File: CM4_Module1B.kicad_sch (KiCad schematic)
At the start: 11 parts, among them J5 2340901-1

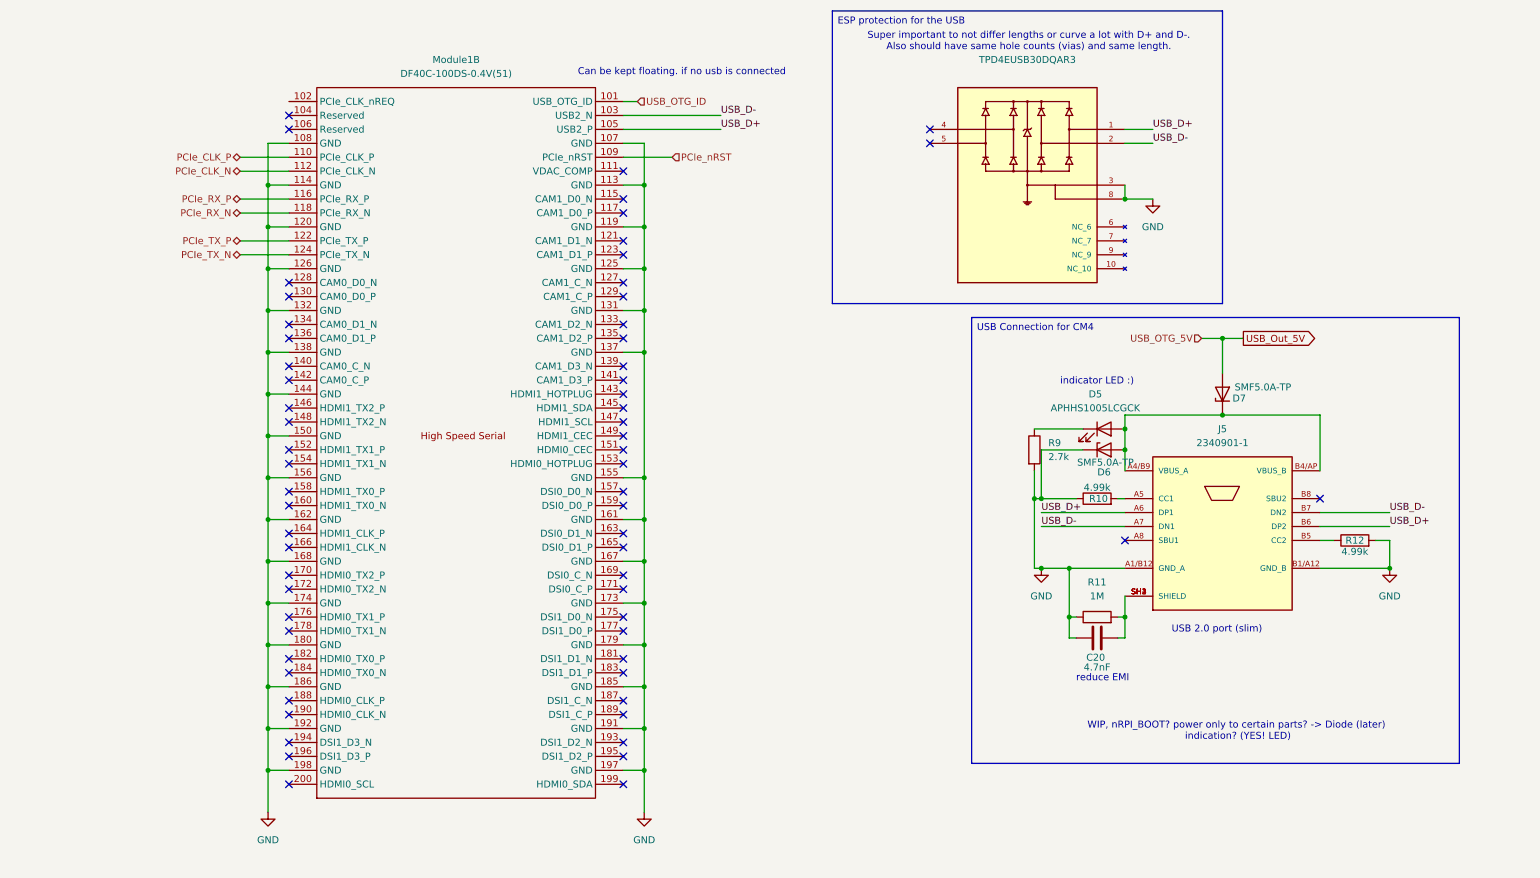
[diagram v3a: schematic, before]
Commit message: tried to find some placements for power routing
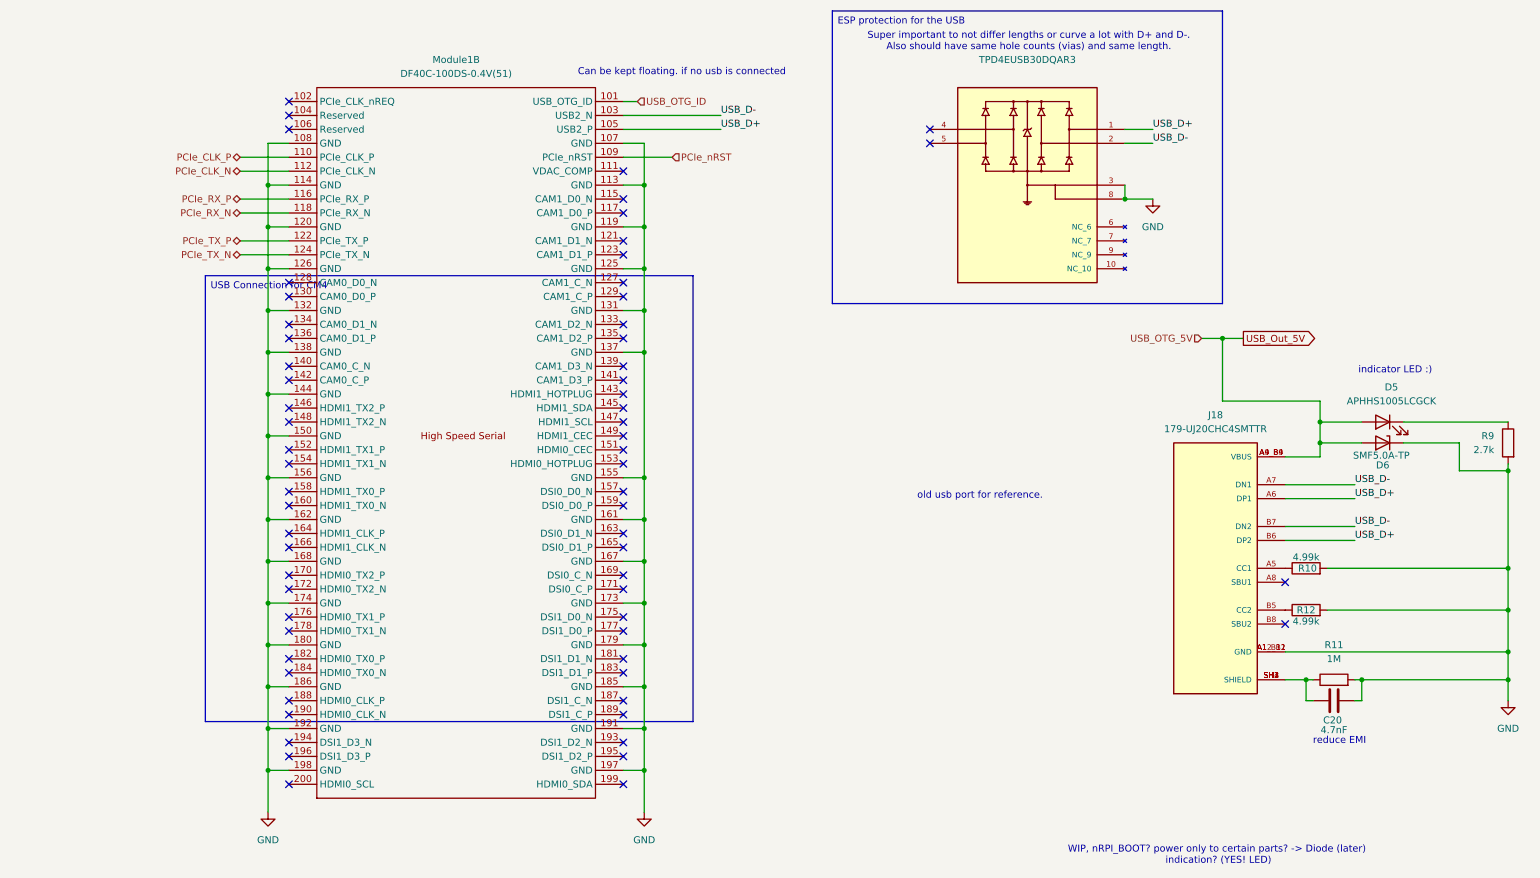
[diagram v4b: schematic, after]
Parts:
- removed D7: SMF5.0A-TP, dz_dio:SMF50ATP, symbol #dzdb:s_dio/D-MCC-SMF5.0A-TP
- removed J5: 2340901-1, dz_con:CON-TECON-2340901-1, symbol #dzdb:s_con/CON-TEC-2340901-1
- added J18: 179-UJ20CHC4SMTTR, dz_con:CON_Samesky_CUI_UJ20-C-H-C-4-SMT-TR, symbol #dzdb:s_con/SAME-179-UJ20CHC4SMTTR
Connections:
- net GND: now also C20.1, R10.2, R11.2, J18.A12_B1 (GND), J18.A1_B12 (GND); no longer C20.2, R10.1, R11.1
- net USB_D+: now also J18.A6 (DP1), J18.B6 (DP2)
- net USB_D-: now also J18.A7 (DN1), J18.B7 (DN2)
- net USB_Out_5V: now also D5.2 (A), D6.2 (A), J18.A4_B9 (VBUS), J18.A9_B4 (VBUS)
- net at R12.1: now also J18.B5 (CC2)
- new net: C20.2, J18.SH1 (SHIELD), J18.SH2 (SHIELD), J18.SH3 (SHIELD), J18.SH4 (SHIELD), R11.1
- new net: J18.A5 (CC1), R10.1
- no-connect marks 63 -> 64
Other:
- note added: "old usb port for reference."
- note removed: "USB 2.0 port (slim)"
- moved on the sheet: C20, D5, D6, R10, R11, R12, R9

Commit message: checked the whole schematic with the datasheet, took notes/questions in the datasheet (pdf also uploaded)
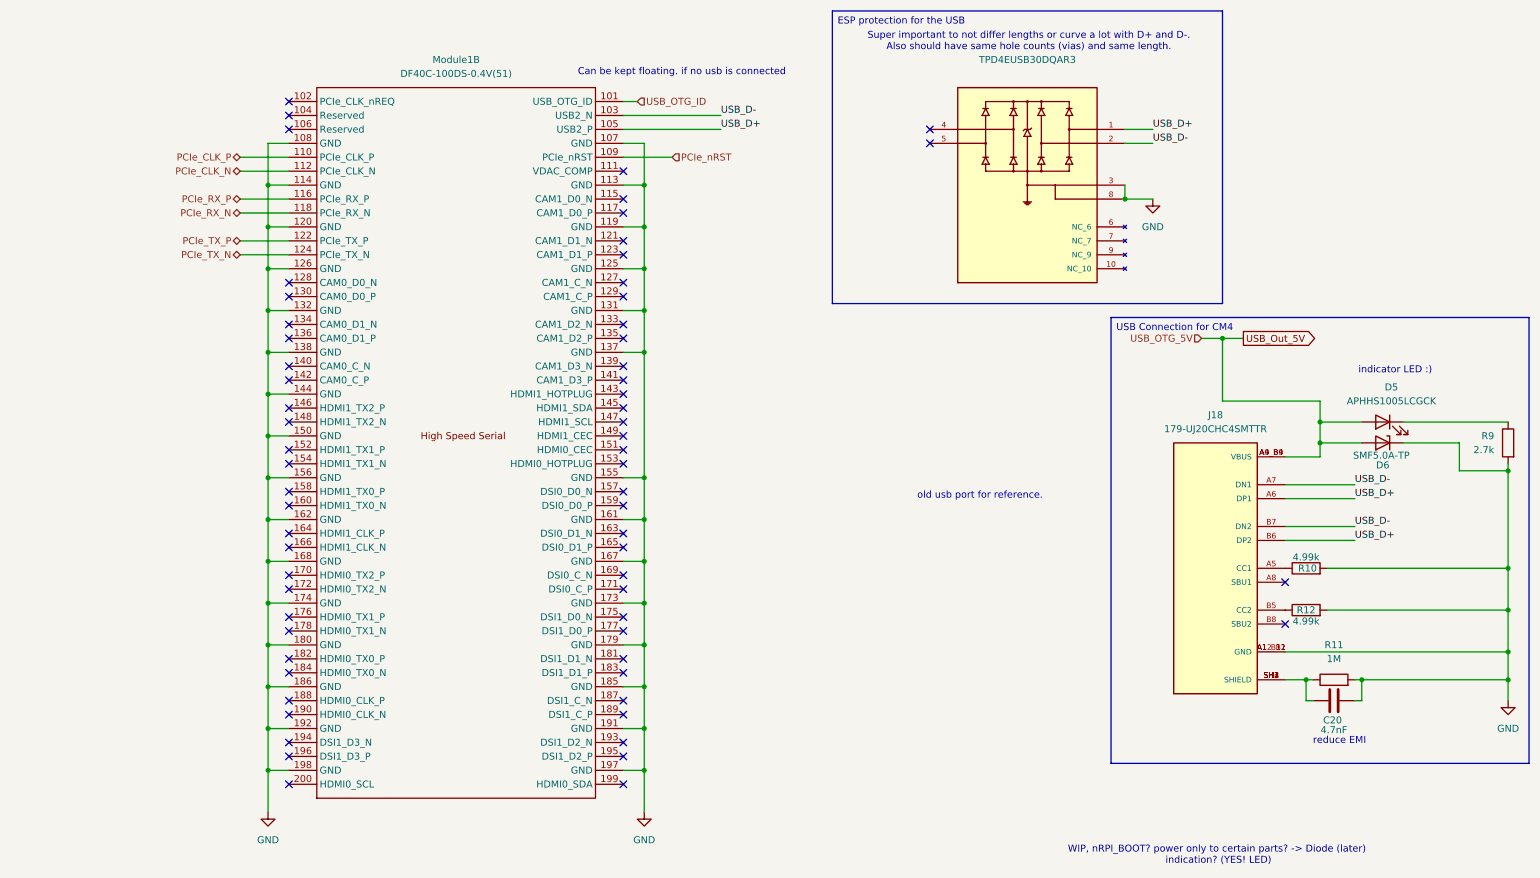
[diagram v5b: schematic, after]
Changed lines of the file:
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@@
 	(text_box "USB Connection for CM4"
 		(exclude_from_sim no)
-		(at 43.18 66.04 0)
-		(size 88.9 81.28)
+		(at 208.28 73.66 0)
+		(size 76.2 81.28)
 		(margins 0.9525 0.9525 0.9525 0.9525)
 		(stroke

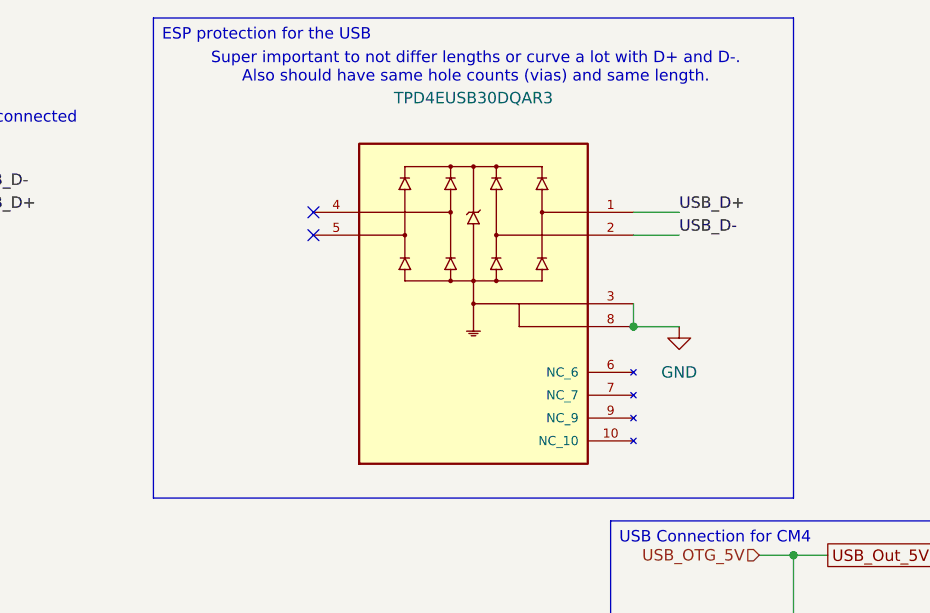
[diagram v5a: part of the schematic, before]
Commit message: multiple changes to the differential pair for easier routing later.
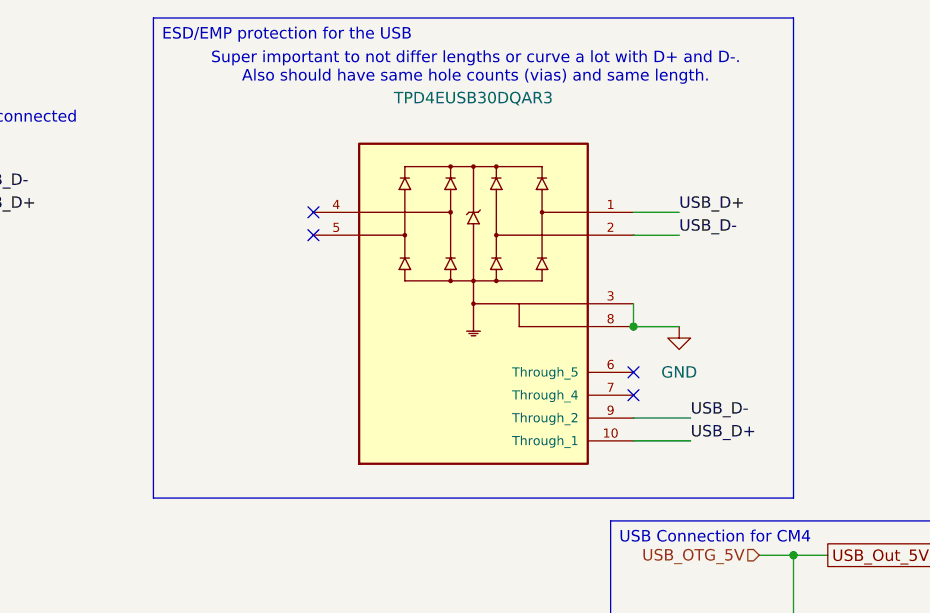
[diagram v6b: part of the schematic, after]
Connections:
- net USB_D+: now also TPD4EUSB30DQAR3.10 (Through_1)
- net USB_D-: now also TPD4EUSB30DQAR3.9 (Through_2)
- no-connect marks 64 -> 66
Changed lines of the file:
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@@
 		)
 	)
-	(text_box "ESP protection for the USB"
+	(text_box "ESD/EMP protection for the USB"
 		(exclude_from_sim no)
 		(at 157.48 17.78 0)
@@
 	)
 	(no_connect
+		(at 210.82 59.69)
+	)
+	(no_connect
 		(at 58.42 128.27)
 	)
@@
 	)
 	(no_connect
+		(at 210.82 57.15)
+	)
+	(no_connect
 		(at 58.42 92.71)
 	)
@@
 	(wire
 		(pts
+			(xy 210.82 62.23) (xy 217.17 62.23)
+		)
+		(stroke
+			(width 0)
+			(type default)
+		)
+	)
+	(wire
+		(pts
 			(xy 119.38 44.45) (xy 128.27 44.45)
 		)
@@
 		(pts
 			(xy 271.78 96.52) (xy 271.78 101.6)
+		)
+		(stroke
+			(width 0)
+			(type default)
+		)
+	)
+	(wire
+		(pts
+			(xy 210.82 64.77) (xy 217.17 64.77)
 		)
 		(stroke
@@
 		)
 	)
+	(label "USB_D-"
+		(at 217.17 62.23 0)
+		(effects
+			(font
+				(size 1.27 1.27)
+			)
+			(justify left bottom)
+		)
+	)
 	(label "USB_D+"
 		(at 252.73 106.68 0)
@@
 		(effects
 			(font
+				(size 1.27 1.27)
+			)
+			(justify left bottom)
+		)
+	)
+	(label "USB_D+"
+		(at 217.17 64.77 0)
+		(effects
+			(font

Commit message: added Gyroscope and Accelerometer part (4x) over IIC
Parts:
- D6: MPN SMF5.0A-TP -> 833-SMF5.0A-TP
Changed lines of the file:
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@@
 			)
 		)
-		(property "MPN" "SMF5.0A-TP"
+		(property "MPN" "833-SMF5.0A-TP"
 			(at 257.81 96.52 0)
 			(effects

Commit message: multiple chainges on PCB
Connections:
- net GND: now also D6.2 (A); no longer D6.1 (K)
- net USB_D+: now also TPD4EUSB30DQAR3.2, TPD4EUSB30DQAR3.9 (Through_2)
- net USB_D-: now also TPD4EUSB30DQAR3.4, TPD4EUSB30DQAR3.5, TPD4EUSB30DQAR3.6 (Through_5), TPD4EUSB30DQAR3.7 (Through_4); no longer TPD4EUSB30DQAR3.2, TPD4EUSB30DQAR3.9 (Through_2)
- net USB_Out_5V: now also D6.1 (K); no longer D6.2 (A)
- no-connect marks 66 -> 62
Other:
- note added: "maybe RX and TX need to be switched"
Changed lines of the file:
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@@
 		)
 	)
+	(text "maybe RX and TX need to be switched"
+		(exclude_from_sim no)
+		(at 29.464 56.896 0)
+		(effects
+			(font
+				(size 1.27 1.27)
+			)
+		)
+	)
 	(text "indicator LED :)"
 		(exclude_from_sim no)
@@
 	)
 	(no_connect
-		(at 210.82 59.69)
-	)
-	(no_connect
 		(at 58.42 128.27)
 	)
@@
 	)
 	(no_connect
-		(at 175.26 39.37)
-	)
-	(no_connect
 		(at 58.42 130.81)
 	)
 	(no_connect
-		(at 210.82 57.15)
-	)
-	(no_connect
 		(at 58.42 92.71)
 	)
@@
 	)
 	(no_connect
-		(at 175.26 41.91)
-	)
-	(no_connect
 		(at 58.42 34.29)
 	)
@@
 	(wire
 		(pts
-			(xy 210.82 62.23) (xy 217.17 62.23)
-		)
-		(stroke
-			(width 0)
-			(type default)
-		)
-	)
-	(wire
-		(pts
 			(xy 119.38 44.45) (xy 128.27 44.45)
 		)
@@
 	(wire
 		(pts
-			(xy 210.82 64.77) (xy 217.17 64.77)
-		)
-		(stroke
-			(width 0)
-			(type default)
-		)
-	)
-	(wire
-		(pts
 			(xy 54.61 95.25) (xy 54.61 87.63)
 		)
@@
 	(wire
 		(pts
-			(xy 210.82 39.37) (xy 215.9 39.37)
-		)
-		(stroke
-			(width 0)
-			(type default)
-		)
-	)
-	(wire
-		(pts
 			(xy 240.03 104.14) (xy 252.73 104.14)
 		)
@@
 	(wire
 		(pts
-			(xy 210.82 41.91) (xy 215.9 41.91)
-		)
-		(stroke
-			(width 0)
-			(type default)
-		)
-	)
-	(wire
-		(pts
 			(xy 240.03 139.7) (xy 243.84 139.7)
 		)
@@
 	(wire
 		(pts
-			(xy 210.82 52.07) (xy 215.9 52.07)
+			(xy 210.82 52.07) (xy 224.79 52.07)
 		)
 		(stroke
@@
 		)
 	)
-	(label "USB_D-"
-		(at 217.17 62.23 0)
+	(label "USB_D+"
+		(at 210.82 41.91 0)
 		(effects
 			(font
@@
 	)
 	(label "USB_D+"
+		(at 210.82 64.77 0)
+		(effects
+			(font
+				(size 1.27 1.27)
+			)
+			(justify left bottom)
+		)
+	)
+	(label "USB_D+"
 		(at 252.73 114.3 0)
 		(effects
@@
 		)
 	)
+	(label "USB_D-"
+		(at 175.26 41.91 180)
+		(effects
+			(font
+				(size 1.27 1.27)
+			)
+			(justify right bottom)
+		)
+	)
 	(label "USB_D+"
-		(at 215.9 39.37 0)
+		(at 210.82 39.37 0)
 		(effects
 			(font
@@
 	)
 	(label "USB_D-"
-		(at 215.9 41.91 0)
+		(at 210.82 57.15 0)
 		(effects
 			(font
@@
 		)
 	)
-	(label "USB_D+"
-		(at 217.17 64.77 0)
+	(label "USB_D-"
+		(at 210.82 59.69 0)
 		(effects
 			(font
@@
 		)
 	)
+	(label "USB_D+"
+		(at 210.82 62.23 0)
+		(effects
+			(font
+				(size 1.27 1.27)
+			)
+			(justify left bottom)
+		)
+	)
+	(label "USB_D-"
+		(at 175.26 39.37 180)
+		(effects
+			(font
+				(size 1.27 1.27)
+			)
+			(justify right bottom)
+		)
+	)
 	(label "USB_D-"
 		(at 252.73 104.14 0)
@@
 		(lib_id "#dzdb:s_dio/D-MCC-SMF5.0A-TP")
 		(at 257.81 96.52 0)
-		(mirror y)
 		(unit 1)
 		(exclude_from_sim no)
@@
 		)
 		(property "Value" "SMF5.0A-TP"
-			(at 257.556 98.806 0)
+			(at 258.064 98.806 0)
 			(effects
 				(font
@@
 	(symbol
 		(lib_id "power:GND")
-		(at 215.9 52.07 0)
+		(at 224.79 52.07 0)
 		(unit 1)
 		(exclude_from_sim no)
@@
 		(fields_autoplaced yes)
 		(property "Reference" "#PWR024"
-			(at 215.9 58.42 0)
+			(at 224.79 58.42 0)
 			(effects
 				(font
@@
 		)
 		(property "Value" "GND"
-			(at 215.9 57.15 0)
+			(at 224.79 57.15 0)
 			(effects
 				(font
@@
 		)
 		(property "Footprint" ""
-			(at 215.9 52.07 0)
+			(at 224.79 52.07 0)
 			(effects
 				(font
@@
 		)
 		(property "Datasheet" ""
-			(at 215.9 52.07 0)
+			(at 224.79 52.07 0)
 			(effects
 				(font
@@
 		)
 		(property "Description" "Power symbol creates a global label with name \"GND\" , ground"
-			(at 215.9 52.07 0)
+			(at 224.79 52.07 0)
 			(effects
 				(font
